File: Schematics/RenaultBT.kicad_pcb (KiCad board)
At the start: 2 copper layers, 55 parts, among them Q1 2N7000, Q2 2N7000, Q3 2N7000, Q4 2N7000, U1 LM2576T-5, U2 LM1117-3.3, U3 WM8804, U4 CSRA64215, U5 74HC04, U6 STM32F103, Y1 12Mhz

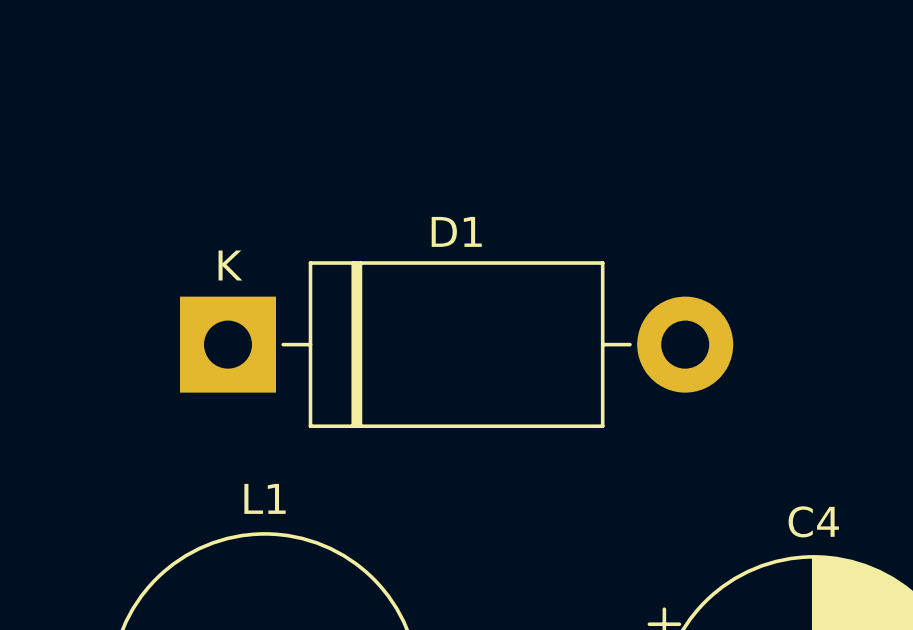
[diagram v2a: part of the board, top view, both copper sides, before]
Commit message: Modified power supply
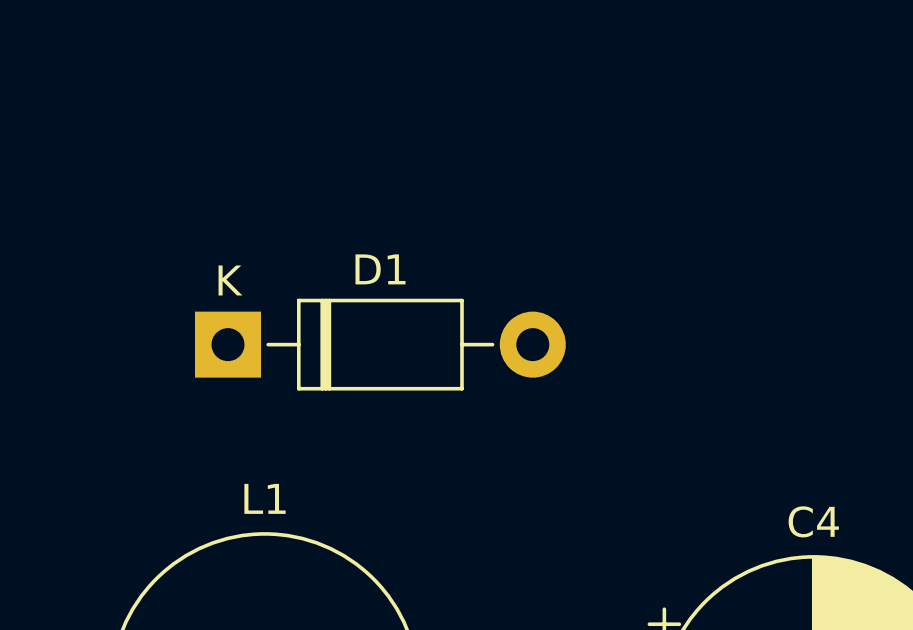
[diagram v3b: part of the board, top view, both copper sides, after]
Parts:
- C2: value 1000uF -> 330uF
- D1: value 1N5822 -> 1N5819; footprint Diode_THT:D_DO-201AD_P15.24mm_Horizontal -> Diode_THT:D_DO-41_SOD81_P10.16mm_Horizontal
- L1: value 100uH -> 330uH
- R1, R2: value 20K -> 10K
- U1: value LM2576T-5 -> LM2575-5.0BT
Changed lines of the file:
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@@
       (effects (font (size 1 1) (thickness 0.15)))
     )
-    (fp_text value 1000uF (at 2.5 6.25) (layer F.Fab)
+    (fp_text value 330uF (at 2.5 6.25) (layer F.Fab)
       (effects (font (size 1 1) (thickness 0.15)))
     )
@@
     )
   )
-  (module Diode_THT:D_DO-201AD_P15.24mm_Horizontal (layer F.Cu)
-    (at 125.73 73.66)
-    (descr "Diode, DO-201AD series, Axial, Horizontal, pin pitch=15.24mm, , length*diameter=9.5*5.2mm^2, , http://www.diodes.com/_files/packages/DO-201AD.pdf")
-    (tags "Diode DO-201AD series Axial Horizontal pin pitch 15.24mm  length 9.5mm diameter 5.2mm")
-    (fp_text reference D1 (at 7.62 -3.72) (layer F.SilkS)
-      (effects (font (size 1 1) (thickness 0.15)))
-    )
-    (fp_text value 1N5822 (at 7.62 3.72) (layer F.Fab)
-      (effects (font (size 1 1) (thickness 0.15)))
-    )
-    (fp_line (start 2.87 -2.6) (end 2.87 2.6) (layer F.Fab) (width 0.1))
-    (fp_line (start 2.87 2.6) (end 12.37 2.6) (layer F.Fab) (width 0.1))
-    (fp_line (start 12.37 2.6) (end 12.37 -2.6) (layer F.Fab) (width 0.1))
-    (fp_line (start 12.37 -2.6) (end 2.87 -2.6) (layer F.Fab) (width 0.1))
-    (fp_line (start 0 0) (end 2.87 0) (layer F.Fab) (width 0.1))
-    (fp_line (start 15.24 0) (end 12.37 0) (layer F.Fab) (width 0.1))
-    (fp_line (start 4.295 -2.6) (end 4.295 2.6) (layer F.Fab) (width 0.1))
-    (fp_line (start 4.395 -2.6) (end 4.395 2.6) (layer F.Fab) (width 0.1))
-    (fp_line (start 4.195 -2.6) (end 4.195 2.6) (layer F.Fab) (width 0.1))
-    (fp_line (start 2.75 -2.72) (end 2.75 2.72) (layer F.SilkS) (width 0.12))
-    (fp_line (start 2.75 2.72) (end 12.49 2.72) (layer F.SilkS) (width 0.12))
-    (fp_line (start 12.49 2.72) (end 12.49 -2.72) (layer F.SilkS) (width 0.12))
-    (fp_line (start 12.49 -2.72) (end 2.75 -2.72) (layer F.SilkS) (width 0.12))
-    (fp_line (start 1.84 0) (end 2.75 0) (layer F.SilkS) (width 0.12))
-    (fp_line (start 13.4 0) (end 12.49 0) (layer F.SilkS) (width 0.12))
-    (fp_line (start 4.295 -2.72) (end 4.295 2.72) (layer F.SilkS) (width 0.12))
-    (fp_line (start 4.415 -2.72) (end 4.415 2.72) (layer F.SilkS) (width 0.12))
-    (fp_line (start 4.175 -2.72) (end 4.175 2.72) (layer F.SilkS) (width 0.12))
-    (fp_line (start -1.85 -2.85) (end -1.85 2.85) (layer F.CrtYd) (width 0.05))
-    (fp_line (start -1.85 2.85) (end 17.09 2.85) (layer F.CrtYd) (width 0.05))
-    (fp_line (start 17.09 2.85) (end 17.09 -2.85) (layer F.CrtYd) (width 0.05))
-    (fp_line (start 17.09 -2.85) (end -1.85 -2.85) (layer F.CrtYd) (width 0.05))
-    (fp_text user %R (at 8.3325 0) (layer F.Fab)
-      (effects (font (size 1 1) (thickness 0.15)))
-    )
-    (fp_text user K (at 0 -2.6) (layer F.Fab)
-      (effects (font (size 1 1) (thickness 0.15)))
-    )
-    (fp_text user K (at 0 -2.6) (layer F.SilkS)
-      (effects (font (size 1 1) (thickness 0.15)))
-    )
-    (pad 1 thru_hole rect (at 0 0) (size 3.2 3.2) (drill 1.6) (layers *.Cu *.Mask)
-      (net 1 "Net-(D1-Pad1)"))
-    (pad 2 thru_hole oval (at 15.24 0) (size 3.2 3.2) (drill 1.6) (layers *.Cu *.Mask)
-      (net 5 /I2SToSPDIF/DGND))
-    (model ${KISYS3DMOD}/Diode_THT.3dshapes/D_DO-201AD_P15.24mm_Horizontal.wrl
-      (at (xyz 0 0 0))
-      (scale (xyz 1 1 1))
-      (rotate (xyz 0 0 0))
-    )
-  )
   (module Inductor_THT:L_Radial_D10.0mm_P5.00mm_Fastron_07M (layer F.Cu)
     (at 124.46 85.09)
@@
       (effects (font (size 1 1) (thickness 0.15)))
     )
-    (fp_text value 100uH (at 2.5 6.25) (layer F.Fab)
+    (fp_text value 330uH (at 2.5 6.25) (layer F.Fab)
       (effects (font (size 1 1) (thickness 0.15)))
     )
@@
       (effects (font (size 1 1) (thickness 0.15)))
     )
-    (fp_text value 20K (at 5.08 2.37 180) (layer F.Fab)
+    (fp_text value 10K (at 5.08 2.37 180) (layer F.Fab)
       (effects (font (size 1 1) (thickness 0.15)))
     )
@@
       (effects (font (size 1 1) (thickness 0.15)))
     )
-    (fp_text value 20K (at 5.08 2.37) (layer F.Fab)
+    (fp_text value 10K (at 5.08 2.37) (layer F.Fab)
       (effects (font (size 1 1) (thickness 0.15)))
     )
@@
       (effects (font (size 1 1) (thickness 0.15)))
     )
-    (fp_text value LM2576T-5 (at 3.4 2.5) (layer F.Fab)
+    (fp_text value LM2575-5.0BT (at 3.4 2.5) (layer F.Fab)
       (effects (font (size 1 1) (thickness 0.15)))
     )
@@
       (at (xyz 0 0 0))
       (scale (xyz 1 1 1))
+      (rotate (xyz 0 0 0))
+    )
+  )
+  (module Diode_THT:D_DO-41_SOD81_P10.16mm_Horizontal (layer F.Cu)
+    (at 125.73 73.66)
+    (descr "Diode, DO-41_SOD81 series, Axial, Horizontal, pin pitch=10.16mm, , length*diameter=5.2*2.7mm^2, , http://www.diodes.com/_files/packages/DO-41%20(Plastic).pdf")
+    (tags "Diode DO-41_SOD81 series Axial Horizontal pin pitch 10.16mm  length 5.2mm diameter 2.7mm")
+    (fp_text reference D1 (at 5.08 -2.47) (layer F.SilkS)
+      (effects (font (size 1 1) (thickness 0.15)))
+    )
+    (fp_text value 1N5819 (at 5.08 2.47) (layer F.Fab)
+      (effects (font (size 1 1) (thickness 0.15)))
+    )
+    (fp_line (start 2.48 -1.35) (end 2.48 1.35) (layer F.Fab) (width 0.1))
+    (fp_line (start 2.48 1.35) (end 7.68 1.35) (layer F.Fab) (width 0.1))
+    (fp_line (start 7.68 1.35) (end 7.68 -1.35) (layer F.Fab) (width 0.1))
+    (fp_line (start 7.68 -1.35) (end 2.48 -1.35) (layer F.Fab) (width 0.1))
+    (fp_line (start 0 0) (end 2.48 0) (layer F.Fab) (width 0.1))
+    (fp_line (start 10.16 0) (end 7.68 0) (layer F.Fab) (width 0.1))
+    (fp_line (start 3.26 -1.35) (end 3.26 1.35) (layer F.Fab) (width 0.1))
+    (fp_line (start 3.36 -1.35) (end 3.36 1.35) (layer F.Fab) (width 0.1))
+    (fp_line (start 3.16 -1.35) (end 3.16 1.35) (layer F.Fab) (width 0.1))
+    (fp_line (start 2.36 -1.47) (end 2.36 1.47) (layer F.SilkS) (width 0.12))
+    (fp_line (start 2.36 1.47) (end 7.8 1.47) (layer F.SilkS) (width 0.12))
+    (fp_line (start 7.8 1.47) (end 7.8 -1.47) (layer F.SilkS) (width 0.12))
+    (fp_line (start 7.8 -1.47) (end 2.36 -1.47) (layer F.SilkS) (width 0.12))
+    (fp_line (start 1.34 0) (end 2.36 0) (layer F.SilkS) (width 0.12))
+    (fp_line (start 8.82 0) (end 7.8 0) (layer F.SilkS) (width 0.12))
+    (fp_line (start 3.26 -1.47) (end 3.26 1.47) (layer F.SilkS) (width 0.12))
+    (fp_line (start 3.38 -1.47) (end 3.38 1.47) (layer F.SilkS) (width 0.12))
+    (fp_line (start 3.14 -1.47) (end 3.14 1.47) (layer F.SilkS) (width 0.12))
+    (fp_line (start -1.35 -1.6) (end -1.35 1.6) (layer F.CrtYd) (width 0.05))
+    (fp_line (start -1.35 1.6) (end 11.51 1.6) (layer F.CrtYd) (width 0.05))
+    (fp_line (start 11.51 1.6) (end 11.51 -1.6) (layer F.CrtYd) (width 0.05))
+    (fp_line (start 11.51 -1.6) (end -1.35 -1.6) (layer F.CrtYd) (width 0.05))
+    (fp_text user %R (at 5.47 0) (layer F.Fab)
+      (effects (font (size 1 1) (thickness 0.15)))
+    )
+    (fp_text user K (at 0 -2.1) (layer F.Fab)
+      (effects (font (size 1 1) (thickness 0.15)))
+    )
+    (fp_text user K (at 0 -2.1) (layer F.SilkS)
+      (effects (font (size 1 1) (thickness 0.15)))
+    )
+    (pad 1 thru_hole rect (at 0 0) (size 2.2 2.2) (drill 1.1) (layers *.Cu *.Mask)
+      (net 1 "Net-(D1-Pad1)"))
+    (pad 2 thru_hole oval (at 10.16 0) (size 2.2 2.2) (drill 1.1) (layers *.Cu *.Mask)
+      (net 5 /I2SToSPDIF/DGND))
+    (model ${KISYS3DMOD}/Diode_THT.3dshapes/D_DO-41_SOD81_P10.16mm_Horizontal.wrl
+      (at (xyz 0 0 0))
+      (scale (xyz 1 1 1))

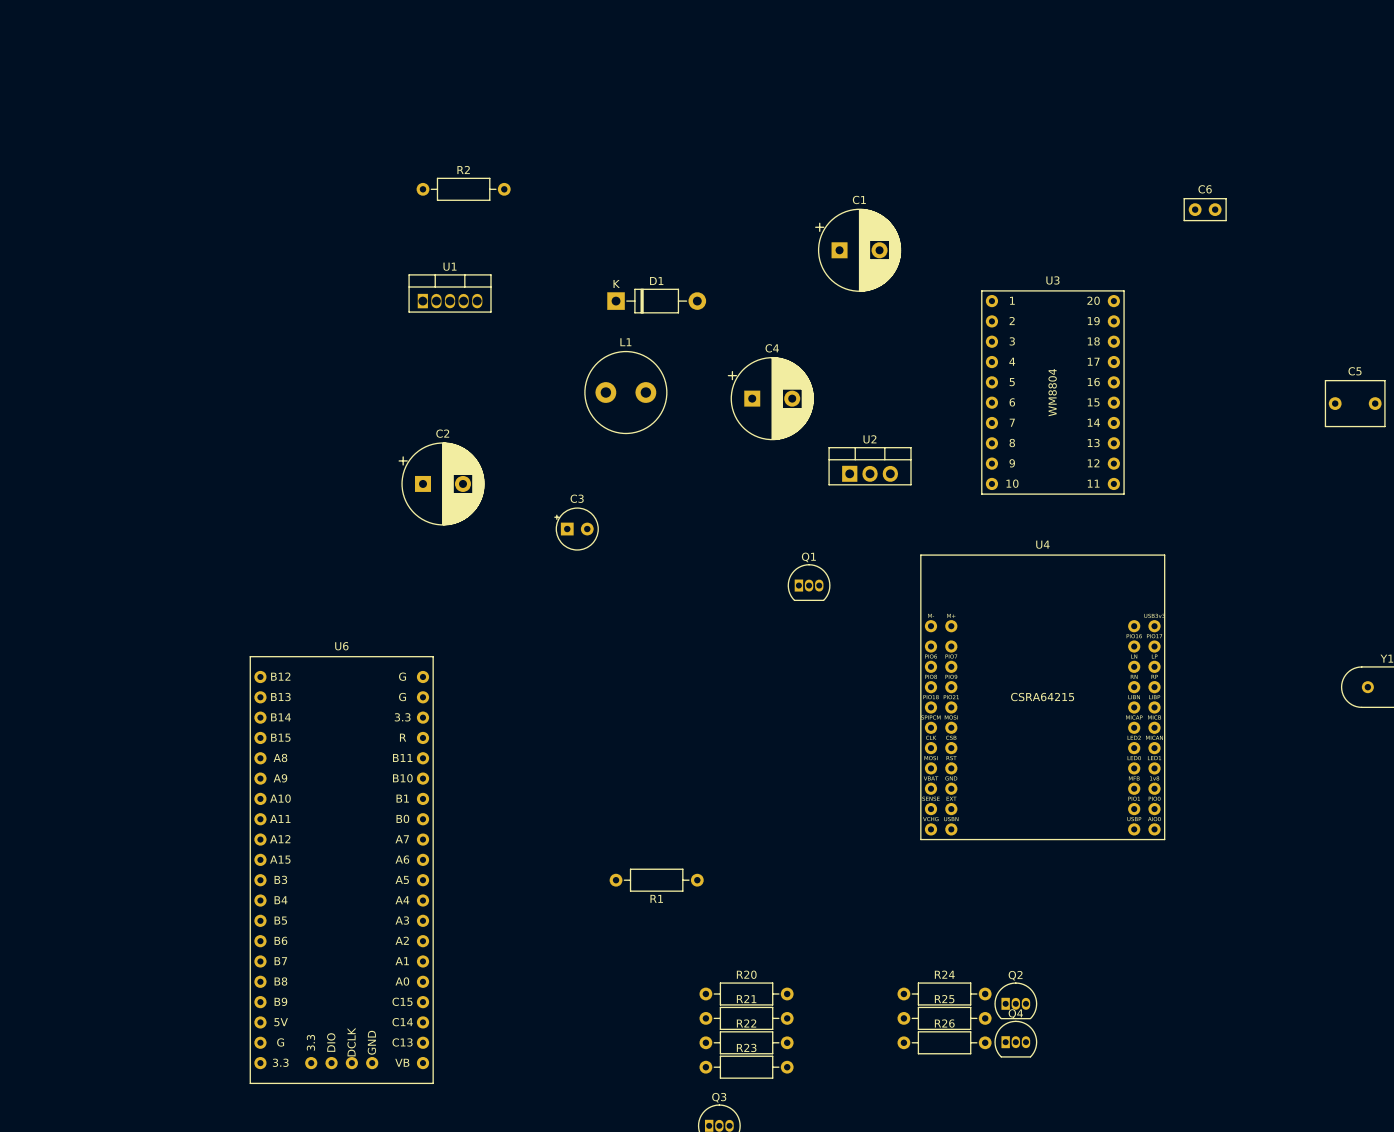
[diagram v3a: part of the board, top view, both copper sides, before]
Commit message: Fixed library path errors; added edge-cut for PCB; added screw connector to the schematic
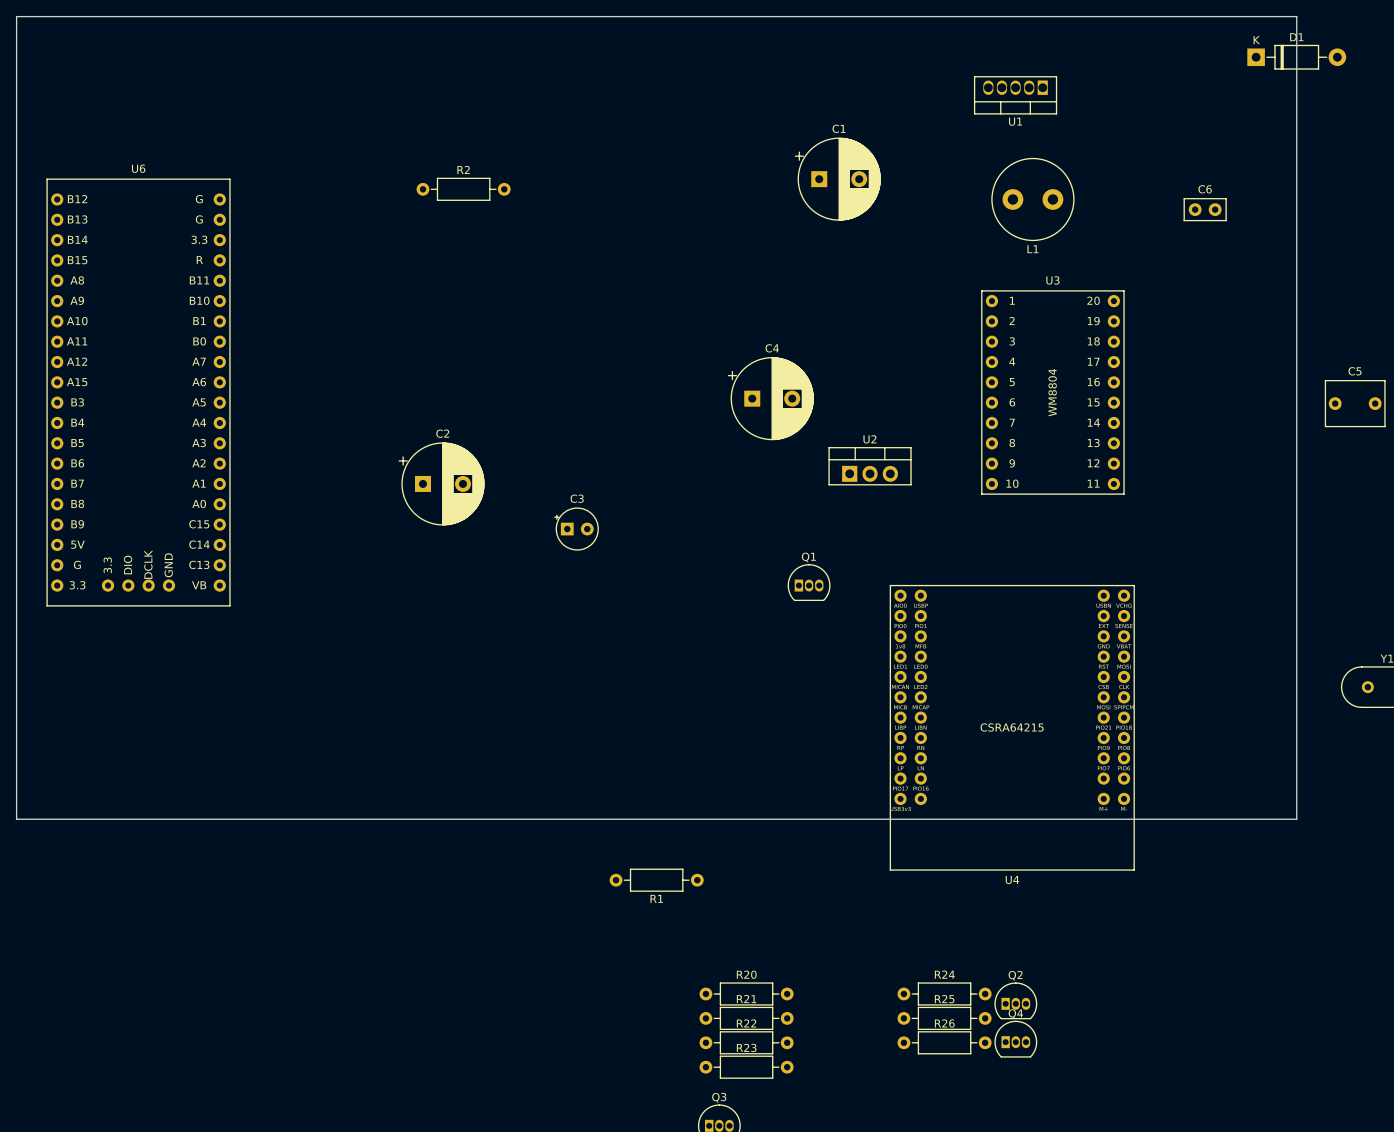
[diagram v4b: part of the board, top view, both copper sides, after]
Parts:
- moved D1 85.6 mm to (205.7, 43.2)
- moved U1 82.0 mm to (179.1, 47.0), turned to 180 degrees
- moved U6 64.9 mm to (66.0, 85.1)
- moved L1 60.9 mm to (180.3, 61.0), turned to 180 degrees
- moved C1 9.25 mm to (151.1, 58.4)
- moved U4 5.39 mm to (175.3, 127.0), turned to 180 degrees
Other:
- board outline added: 160 x 100.3 mm

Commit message: Added foorprint for screw terminals; simplified power supply; PCB partial design
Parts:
- removed C3: 10uF, Capacitor_THT:CP_Radial_Tantal_D5.0mm_P2.50mm
- added J1: PowerSupply, ScrewTerminal:ScrewTerminal_3, F.Cu at (203.2, 49.5)
- added J2: SPDIF_Output, ScrewTerminal:ScrewTerminal_2, F.Cu at (203.2, 129.5)
- added J3: HU_CDC_Interface, ScrewTerminal:ScrewTerminal_2, F.Cu at (203.2, 115.6)
- C2: value 330uF -> 470uF
- moved JP1 147.5 mm to (135.9, 125.7), turned to 270 degrees
- moved JP7 144.5 mm to (135.9, 113.0), turned to 270 degrees
- moved JP3 141.2 mm to (135.9, 120.7), turned to 270 degrees
- moved JP4 138.8 mm to (135.9, 123.2), turned to 270 degrees
- moved JP5 136.7 mm to (135.9, 118.1), turned to 270 degrees
- moved JP6 134.6 mm to (135.9, 115.6), turned to 270 degrees
- moved JP2 131.6 mm to (135.9, 128.3), turned to 270 degrees
- moved R8 124.6 mm to (113.0, 86.4), turned to 180 degrees
- moved R7 112.4 mm to (156.2, 142.2)
- moved R23 106.8 mm to (95.2, 71.1), turned to 180 degrees
- moved R22 106.2 mm to (85.1, 73.7)
- moved R1 103.5 mm to (186.7, 55.9)
- moved R14 101.9 mm to (133.3, 142.2)
- moved R20 100.7 mm to (53.3, 104.1), turned to 90 degrees
- moved C7 99.1 mm to (144.8, 109.2), turned to 180 degrees
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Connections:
- Q2 pad 3: (no net) -> /HU_CDC_InterfaceAdapter/HU_RX
- Q4 pad 2: (no net) -> /HU_CDC_InterfaceAdapter/HU_TX
